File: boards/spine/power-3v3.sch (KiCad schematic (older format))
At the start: 13 parts

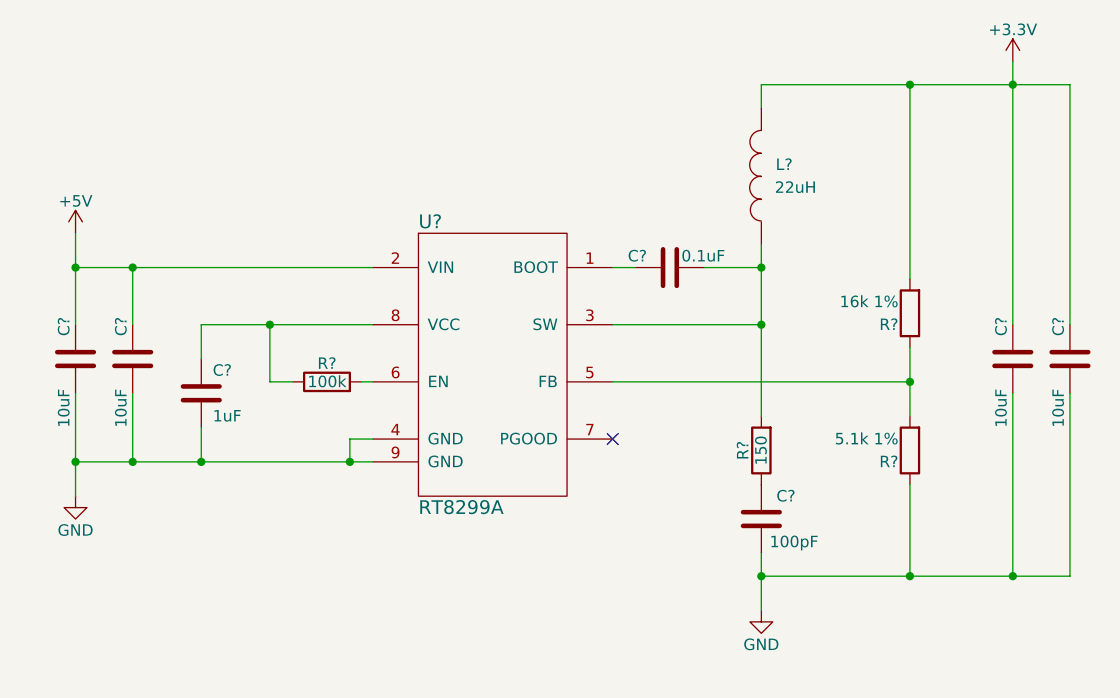
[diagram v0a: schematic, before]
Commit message: Power source switching
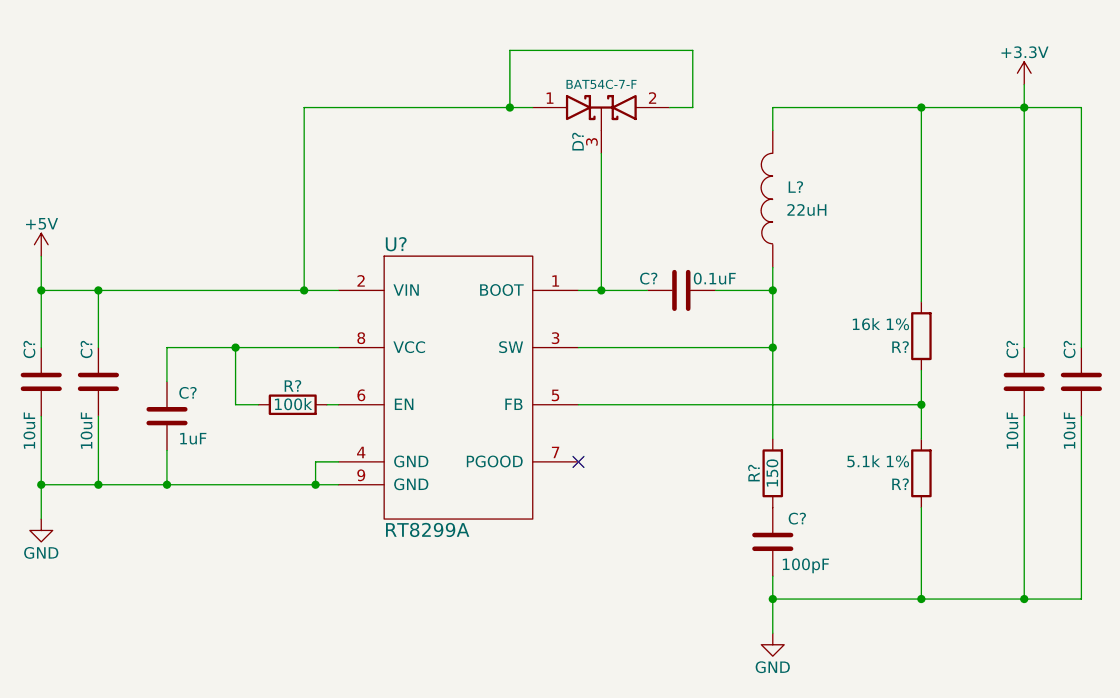
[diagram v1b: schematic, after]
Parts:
- added D?: BAT54 2x common cathode, symbol D_Schottky_x2_KCom_AAK
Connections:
- net +5V: now also D?.1 (A), D?.2 (A)
- net at C?.2, U?.1 (BOOT): now also D?.3 (K)
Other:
- moved on the sheet: C?, L?, R?, U?

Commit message: Power management and such
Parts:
- gave numbers to parts that had none: 14
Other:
- note added: "Bootstrap assistance diode;\nsee RT8299A data sheet"
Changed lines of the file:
@@
 $EndDescr
 $Comp
-L R R?
+L R R25
 U 1 1 564CF3B2
 P 4400 4300
-F 0 "R?" V 4480 4300 50  0000 C CNN
+F 0 "R25" V 4480 4300 50  0000 C CNN
 F 1 "100k" V 4400 4300 50  0000 C CNN
 F 2 "" V 4330 4300 30  0000 C CNN
@@
 $EndComp
 $Comp
-L GND #PWR?
+L GND #PWR0126
 U 1 1 564CF3B3
 P 3300 4800
-F 0 "#PWR?" H 3300 4550 50  0001 C CNN
+F 0 "#PWR0126" H 3300 4550 50  0001 C CNN
 F 1 "GND" H 3300 4650 50  0000 C CNN
 F 2 "" H 3300 4800 60  0000 C CNN
@@
 $EndComp
 $Comp
-L C C?
+L C C55
 U 1 1 564CF3B4
 P 3300 4200
-F 0 "C?" V 3250 4300 50  0000 L CNN
+F 0 "C55" V 3250 4300 50  0000 L CNN
 F 1 "10uF " V 3250 3900 50  0000 L CNN
 F 2 "1206" H 3338 4050 30  0001 C CNN
@@
 $EndComp
 $Comp
-L C C?
+L C C57
 U 1 1 564CF3B6
 P 3850 4350
-F 0 "C?" H 3900 4450 50  0000 L CNN
+F 0 "C57" H 3900 4450 50  0000 L CNN
 F 1 "1uF " H 3900 4250 50  0000 L CNN
 F 2 "0805" H 3888 4200 30  0001 C CNN
@@
 $EndComp
 $Comp
-L RT8299A U?
+L RT8299A U9
 U 1 1 564CF3B7
 P 5050 3600
-F 0 "U?" H 4800 3600 60  0000 L CNN
+F 0 "U9" H 4800 3600 60  0000 L CNN
 F 1 "RT8299A" H 4800 2350 60  0000 L CNN
 F 2 "8-SOP-EP" H 5050 3600 60  0001 C CNN
@@
 $EndComp
 $Comp
-L C C?
+L C C58
 U 1 1 564CF3B8
 P 6100 3800
-F 0 "C?" V 6050 3700 50  0000 R CNN
+F 0 "C58" V 6050 3700 50  0000 R CNN
 F 1 "0.1uF" V 6050 3850 50  0000 L CNN
 F 2 "0805" H 6138 3650 30  0001 C CNN
@@
 $EndComp
 $Comp
-L INDUCTOR L?
+L INDUCTOR L2
 U 1 1 564CF3B9
 P 6500 3400
-F 0 "L?" H 6400 3350 50  0000 C CNN
+F 0 "L2" H 6400 3350 50  0000 C CNN
 F 1 "22uH" H 6350 3450 50  0000 C CNN
 F 2 "" H 6500 3400 60  0000 C CNN
@@
 $EndComp
 $Comp
-L R R?
+L R R26
 U 1 1 564CF3BA
 P 6500 4600
-F 0 "R?" V 6580 4600 50  0000 C CNN
+F 0 "R26" V 6580 4600 50  0000 C CNN
 F 1 "150" V 6500 4600 50  0000 C CNN
 F 2 "" V 6430 4600 30  0000 C CNN
@@
 $EndComp
 $Comp
-L C C?
+L C C59
 U 1 1 564CF3BB
 P 6500 4900
-F 0 "C?" H 6350 4800 50  0000 L CNN
+F 0 "C59" H 6350 4800 50  0000 L CNN
 F 1 "100pF" H 6250 5000 50  0000 L CNN
 F 2 "0805" H 6538 4750 30  0001 C CNN
@@
 $EndComp
 Wire Wire Line
-	5650 3800 5750 3800
-Wire Wire Line
-	5750 3800 5950 3800
+	5650 3800 5950 3800
 Wire Wire Line
 	4600 4550 4500 4550
@@
 	4500 4550 4500 4650
 Wire Wire Line
-	3300 4650 3550 4650
-Wire Wire Line
-	3550 4650 3850 4650
-Wire Wire Line
-	3850 4650 4500 4650
-Wire Wire Line
-	4500 4650 4600 4650
+	3300 4650 4600 4650
 Connection ~ 4500 4650
 Wire Wire Line
-	3300 4350 3300 4650
-Wire Wire Line
-	3300 4650 3300 4800
+	3300 4350 3300 4800
 Connection ~ 3300 4650
 Wire Wire Line
@@
 Connection ~ 3550 4650
 Wire Wire Line
-	3300 3800 3550 3800
-Wire Wire Line
-	3550 3800 4450 3800
-Wire Wire Line
-	4450 3800 4600 3800
+	3300 3800 4600 3800
 Wire Wire Line
 	3550 3800 3550 4050
 Wire Wire Line
-	3300 3650 3300 3800
-Wire Wire Line
-	3300 3800 3300 4050
+	3300 3650 3300 4050
 Connection ~ 3550 3800
 Connection ~ 3300 3800
@@
 Connection ~ 3850 4650
 Wire Wire Line
-	3850 4050 4150 4050
-Wire Wire Line
-	4150 4050 4600 4050
+	3850 4050 4600 4050
 Wire Wire Line
 	3850 4050 3850 4200
@@
 	6250 3800 6500 3800
 Wire Wire Line
-	6500 3700 6500 3800
-Wire Wire Line
-	6500 3800 6500 4050
-Wire Wire Line
-	6500 4050 6500 4450
-$Comp
-L C C?
+	6500 3700 6500 4450
+$Comp
+L C C56
 U 1 1 564CF3BC
 P 3550 4200
-F 0 "C?" V 3500 4300 50  0000 L CNN
+F 0 "C56" V 3500 4300 50  0000 L CNN
 F 1 "10uF " V 3500 3900 50  0000 L CNN
 F 2 "1206" H 3588 4050 30  0001 C CNN
@@
 $EndComp
 $Comp
-L C C?
+L C C60
 U 1 1 564CF3BD
 P 7600 4200
-F 0 "C?" V 7550 4300 50  0000 L CNN
+F 0 "C60" V 7550 4300 50  0000 L CNN
 F 1 "10uF " V 7550 3900 50  0000 L CNN
 F 2 "1206" H 7638 4050 30  0001 C CNN
@@
 $EndComp
 $Comp
-L C C?
+L C C61
 U 1 1 564CF3BE
 P 7850 4200
-F 0 "C?" V 7800 4300 50  0000 L CNN
+F 0 "C61" V 7800 4300 50  0000 L CNN
 F 1 "10uF " V 7800 3900 50  0000 L CNN
 F 2 "1206" H 7888 4050 30  0001 C CNN
@@
 $EndComp
 $Comp
-L R R?
+L R R28
 U 1 1 564CF3BF
 P 7150 4600
-F 0 "R?" H 7200 4650 50  0000 L CNN
+F 0 "R28" H 7200 4650 50  0000 L CNN
 F 1 "5.1k 1%" H 7200 4550 50  0000 L CNN
 F 2 "0805" V 7080 4600 30  0001 C CNN
@@
 $EndComp
 $Comp
-L R R?
+L R R27
 U 1 1 564CF3C0
 P 7150 4000
-F 0 "R?" H 7200 4050 50  0000 L CNN
+F 0 "R27" H 7200 4050 50  0000 L CNN
 F 1 "16k 1%" H 7200 3950 50  0000 L CNN
 F 2 "0805" V 7080 4000 30  0001 C CNN
@@
 $EndComp
 Wire Wire Line
-	7600 2900 7600 3000
-Wire Wire Line
-	7600 3000 7600 4050
+	7600 2900 7600 4050
 Wire Wire Line
 	7850 3000 7850 4050
@@
 	5650 4300 7150 4300
 Wire Wire Line
-	7150 4150 7150 4300
-Wire Wire Line
-	7150 4300 7150 4450
+	7150 4150 7150 4450
 Connection ~ 7150 4300
 Wire Wire Line
@@
 	7150 4750 7150 5150
 Wire Wire Line
-	6500 5150 7150 5150
-Wire Wire Line
-	7150 5150 7600 5150
-Wire Wire Line
-	7600 5150 7850 5150
-Wire Wire Line
-	6500 5050 6500 5150
-Wire Wire Line
-	6500 5150 6500 5300
-$Comp
-L GND #PWR?
+	6500 5150 7850 5150
+Wire Wire Line
+	6500 5050 6500 5300
+$Comp
+L GND #PWR0127
 U 1 1 564CF3C3
 P 6500 5300
-F 0 "#PWR?" H 6500 5050 50  0001 C CNN
+F 0 "#PWR0127" H 6500 5050 50  0001 C CNN
 F 1 "GND" H 6500 5150 50  0000 C CNN
 F 2 "" H 6500 5300 60  0000 C CNN
@@
 NoConn ~ 5650 4550
 $Comp
-L +5V #PWR?
+L +5V #PWR0128
 U 1 1 564CF485
 P 3300 3650
-F 0 "#PWR?" H 3300 3500 50  0001 C CNN
+F 0 "#PWR0128" H 3300 3500 50  0001 C CNN
 F 1 "+5V" H 3300 3790 50  0000 C CNN
 F 2 "" H 3300 3650 60  0000 C CNN
@@
 $EndComp
 $Comp
-L +3.3V #PWR?
+L +3.3V #PWR0129
 U 1 1 564CF4B3
 P 7600 2900
-F 0 "#PWR?" H 7600 2750 50  0001 C CNN
+F 0 "#PWR0129" H 7600 2750 50  0001 C CNN
 F 1 "+3.3V" H 7600 3040 50  0000 C CNN
 F 2 "" H 7600 2900 60  0000 C CNN
@@
 $EndComp
 Wire Wire Line
-	6500 3000 7150 3000
-Wire Wire Line
-	7150 3000 7600 3000
-Wire Wire Line
-	7600 3000 7850 3000
+	6500 3000 7850 3000
 Wire Wire Line
 	7600 5150 7600 4350
@@
 Connection ~ 7600 5150
 $Comp
-L D_Schottky_x2_KCom_AAK D?
+L D_Schottky_x2_KCom_AAK D6
 U 1 1 564CE8A7
 P 5750 3000
-F 0 "D?" V 5650 2850 50  0000 C CNN
+F 0 "D6" V 5650 2850 50  0000 C CNN
 F 1 "BAT54 2x common cathode" H 5750 3100 50  0001 C CNN
 F 2 "" H 5750 3000 60  0000 C CNN
@@
 	5350 2750 5350 3000
 Wire Wire Line
-	4450 3000 5350 3000
-Wire Wire Line
-	5350 3000 5450 3000
+	4450 3000 5450 3000
 Wire Wire Line
 	4450 3000 4450 3800
 Connection ~ 4450 3800
 Connection ~ 5350 3000
+Text Notes 5350 2650 0    60   ~ 0
+Bootstrap assistance diode;\nsee RT8299A data sheet
 $EndSCHEMATC

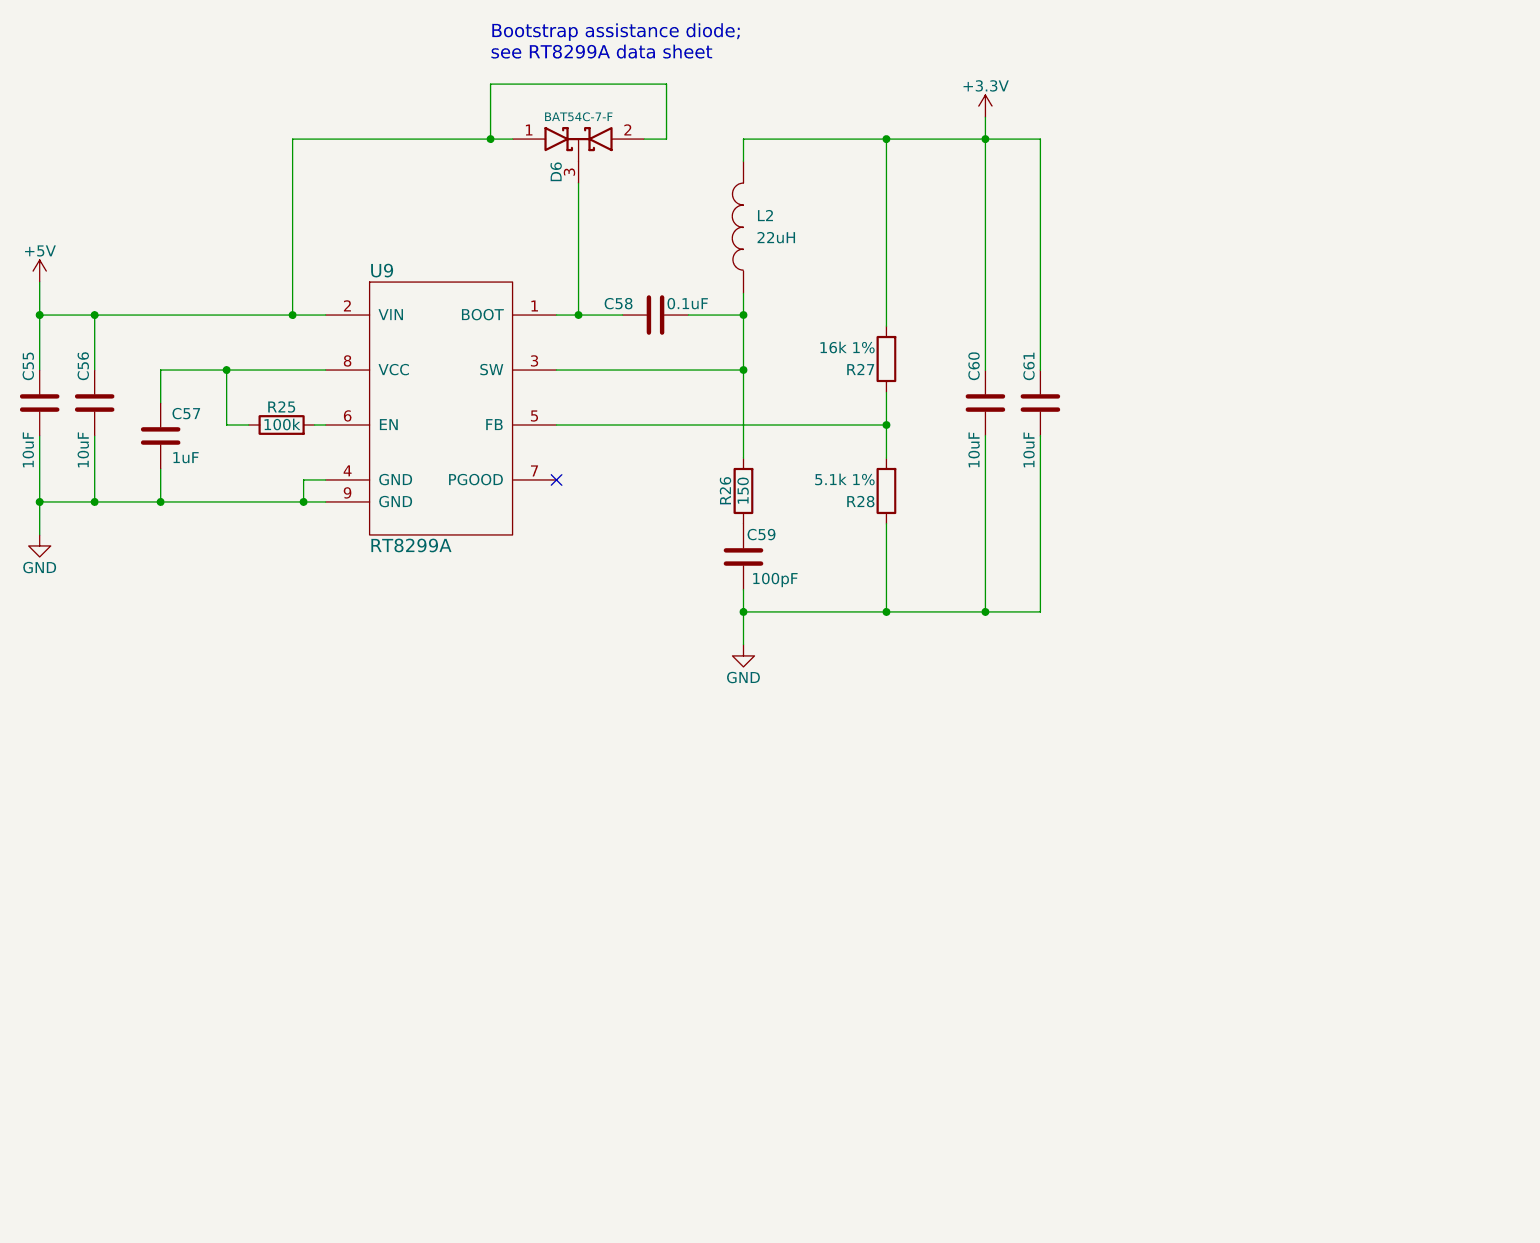
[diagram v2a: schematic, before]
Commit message: Clock generator, sync connectors, title blocks
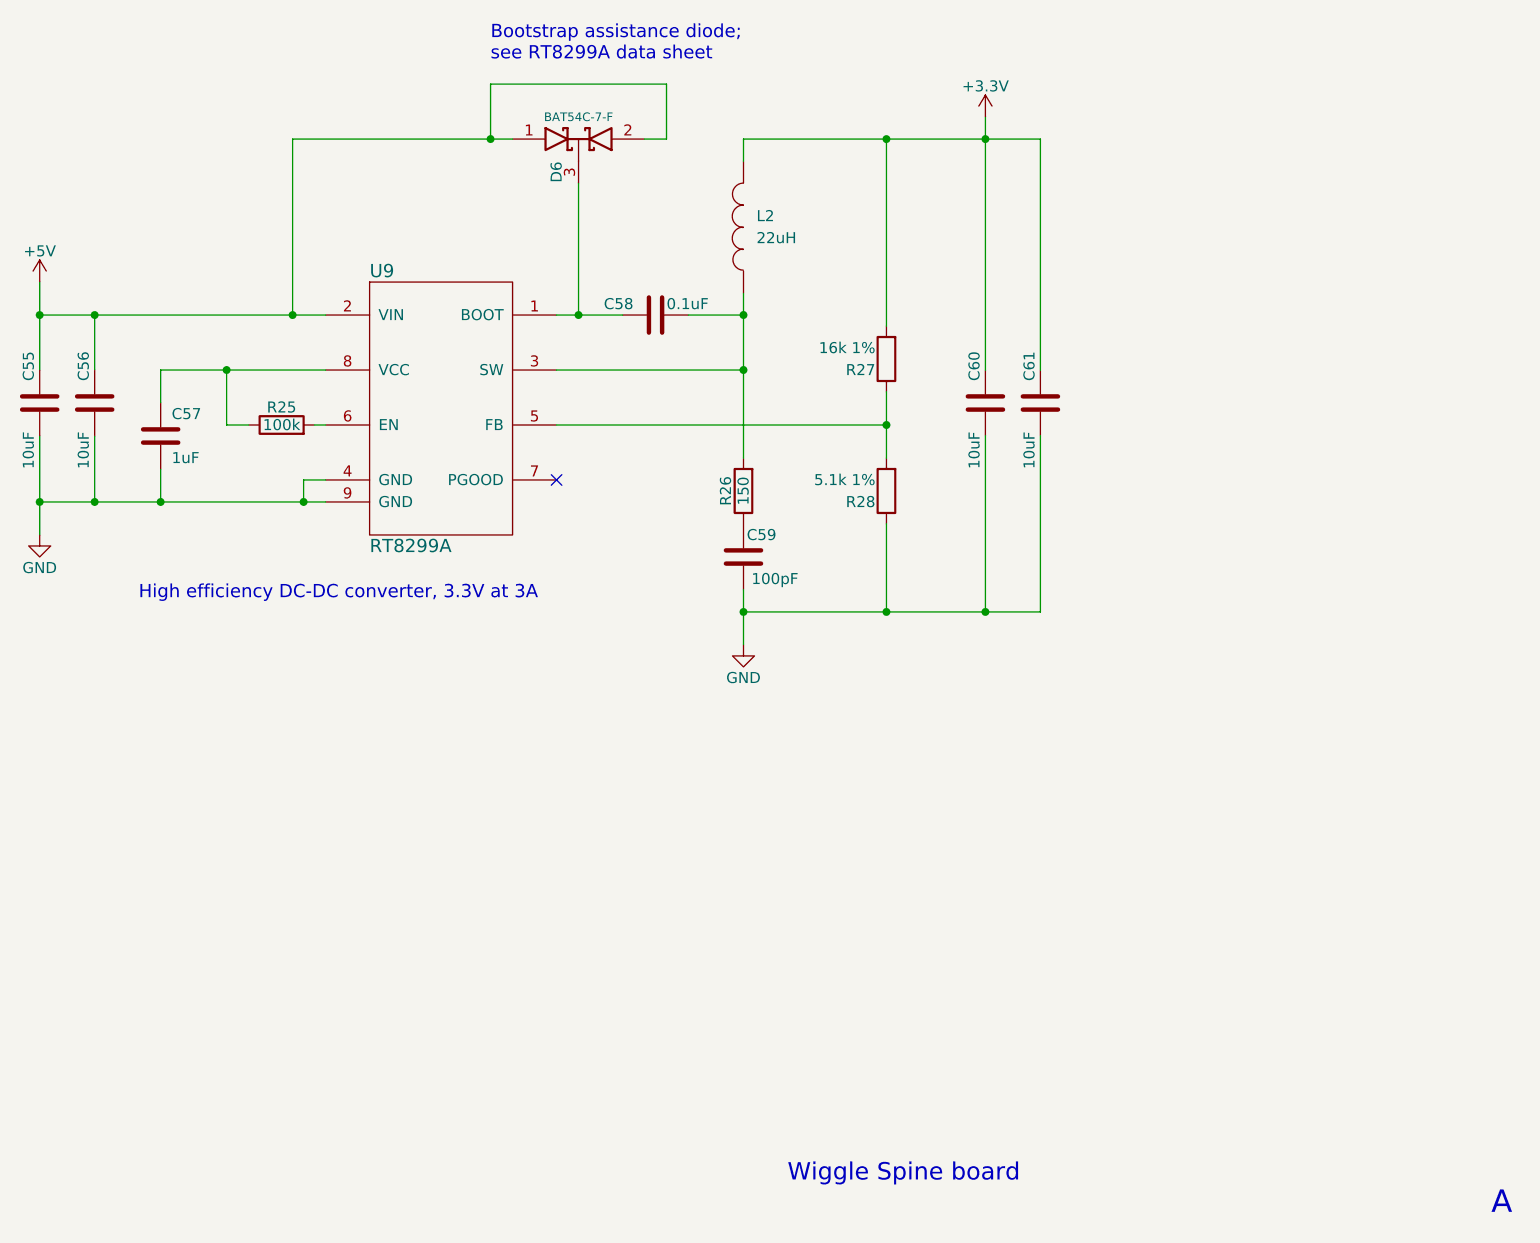
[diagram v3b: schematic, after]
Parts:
- C55, C56, C60, C61: footprint 1206 -> Capacitors_SMD:C_1206
- C57, C58, C59: footprint 0805 -> Capacitors_SMD:C_0805
- R25, R26: footprint (none) -> Resistors_SMD:R_0805
- R27, R28: footprint 0805 -> Resistors_SMD:R_0805
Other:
- note added: "A"
- note added: "High efficiency DC-DC converter, 3.3V at 3A"
- note added: "Wiggle Spine board"

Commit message: Schematic footprint and refdes work
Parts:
- D6: footprint (none) -> TO_SOT_Packages_SMD:SOT-23
- L2: footprint (none) -> Inductors_NEOSID:Neosid_Inductor_SM-NE127
- U9: footprint 8-SOP-EP -> Housings_SOIC:SOIC-8-1EP_3.9x4.9mm_Pitch1.27mm
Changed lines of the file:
@@
 $EndComp
 $Comp
-L GND #PWR0127
+L GND #PWR128
 U 1 1 564CF3B3
 P 3300 4800
-F 0 "#PWR0127" H 3300 4550 50  0001 C CNN
+F 0 "#PWR128" H 3300 4550 50  0001 C CNN
 F 1 "GND" H 3300 4650 50  0000 C CNN
 F 2 "" H 3300 4800 60  0000 C CNN
@@
 F 0 "U9" H 4800 3600 60  0000 L CNN
 F 1 "RT8299A" H 4800 2350 60  0000 L CNN
-F 2 "8-SOP-EP" H 5050 3600 60  0001 C CNN
+F 2 "Housings_SOIC:SOIC-8-1EP_3.9x4.9mm_Pitch1.27mm" H 5050 3600 60  0001 C CNN
 F 3 "http://www.richtek.com/assets/product_file/RT8299A/DS8299A-03.pdf" H 5050 3600 60  0001 C CNN
 F 4 "Digikey" H 5050 3600 60  0001 C CNN "Vend1"
@@
 F 0 "L2" H 6400 3350 50  0000 C CNN
 F 1 "22uH" H 6350 3450 50  0000 C CNN
-F 2 "" H 6500 3400 60  0001 C CNN
+F 2 "Inductors_NEOSID:Neosid_Inductor_SM-NE127" H 6500 3400 60  0001 C CNN
 F 3 "http://www.bourns.com/docs/Product-Datasheets/SRR1280.pdf" H 6500 3400 60  0001 C CNN
 F 4 "SRR1280-220MTR-ND" V 6500 3400 60  0001 C CNN "Vend1Id"
@@
 	6500 5050 6500 5300
 $Comp
-L GND #PWR0128
+L GND #PWR129
 U 1 1 564CF3C3
 P 6500 5300
-F 0 "#PWR0128" H 6500 5050 50  0001 C CNN
+F 0 "#PWR129" H 6500 5050 50  0001 C CNN
 F 1 "GND" H 6500 5150 50  0000 C CNN
 F 2 "" H 6500 5300 60  0000 C CNN
@@
 NoConn ~ 5650 4550
 $Comp
-L +5V #PWR0129
+L +5V #PWR127
 U 1 1 564CF485
 P 3300 3650
-F 0 "#PWR0129" H 3300 3500 50  0001 C CNN
+F 0 "#PWR127" H 3300 3500 50  0001 C CNN
 F 1 "+5V" H 3300 3790 50  0000 C CNN
 F 2 "" H 3300 3650 60  0000 C CNN
@@
 $EndComp
 $Comp
-L +3.3V #PWR0130
+L +3.3V #PWR130
 U 1 1 564CF4B3
 P 7600 2900
-F 0 "#PWR0130" H 7600 2750 50  0001 C CNN
+F 0 "#PWR130" H 7600 2750 50  0001 C CNN
 F 1 "+3.3V" H 7600 3040 50  0000 C CNN
 F 2 "" H 7600 2900 60  0000 C CNN
@@
 F 0 "D6" V 5650 2850 50  0000 C CNN
 F 1 "BAT54 2x common cathode" H 5750 3100 50  0001 C CNN
-F 2 "" H 5750 3000 60  0001 C CNN
+F 2 "TO_SOT_Packages_SMD:SOT-23" H 5750 3000 60  0001 C CNN
 F 3 "http://www.diodes.com/_files/datasheets/ds11005.pdf" H 5750 3000 60  0001 C CNN
 F 4 "Diodes Inc" H 5750 3150 39  0001 C CNN "MfrId"
@@
 72 0F 1C A9 DC 70 49 CB 79 33 88 85 99 AD 01 6C 4B 10 FC 3B 13 DE 3B 37 68 79 AD 07 BC 00 3C 0E
 3C 31 EE E3 D8 E7 0F 03 D7 7B 9F FB C1 E1 FF 01 18 C4 96 1D B8 0E 40 07 00 00 00 00 49 45 4E 44
-AE 42 60 82 00
+AE 42 60 82 2E
 EndData
 $EndBitmap
